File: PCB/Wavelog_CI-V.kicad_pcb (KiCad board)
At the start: 2 copper layers, 28.8 x 55.9 mm, 6 parts, among them SW1 1xUm, X1 CI-V_to_TRX

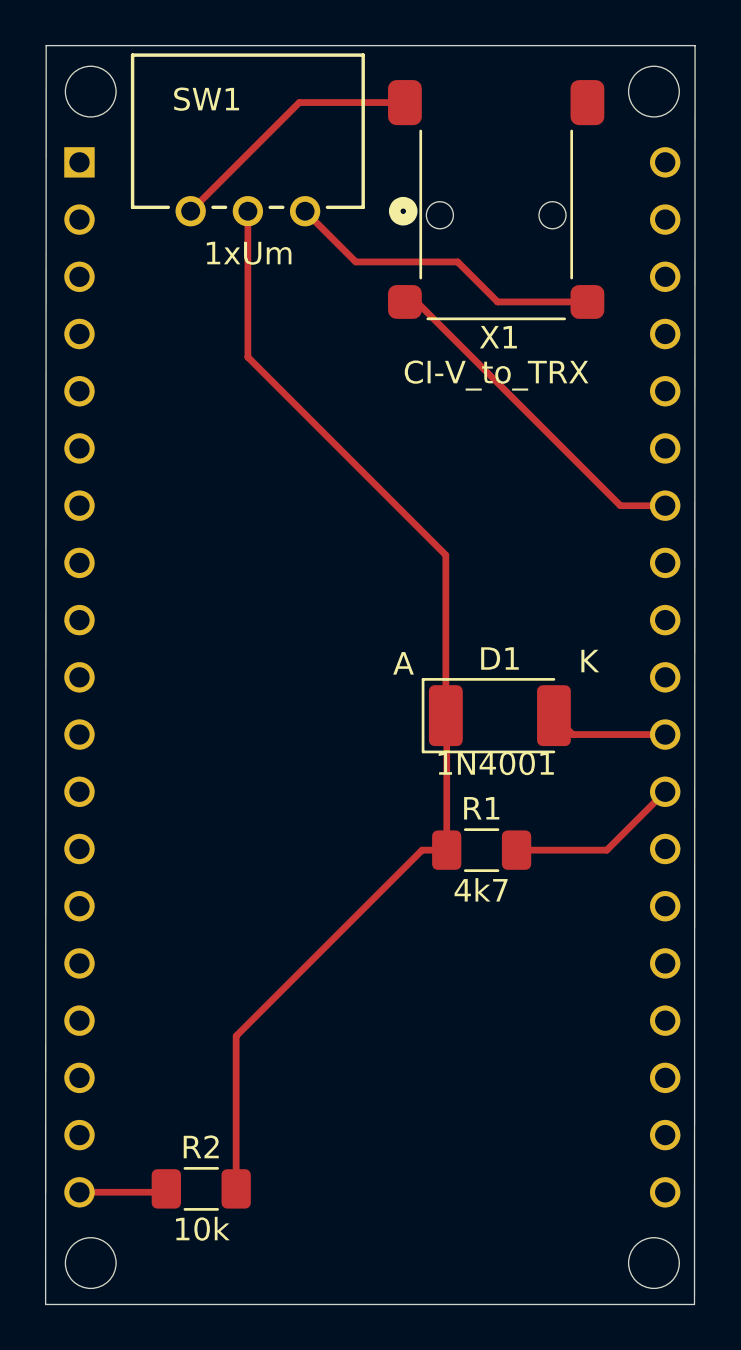
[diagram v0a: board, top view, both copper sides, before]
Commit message: major upgrade PCB v1.2
new features:
++ add 0.96" OLED and RX/TX-LED on PCB and Sketch
++ add rotate button on WebIF for OLED
++ add Autodetect CI-V on Boot
++ add Autodetect button on WebIF
++ add Debug-Level
++ add Debug-Page (last 500 lines or Websocket)
Bugs:
-- Autodetect found no matching address
-- no json-post to WaveLog
-- debug websocket no connection
-- Buffer overflow/Reboot sometimes
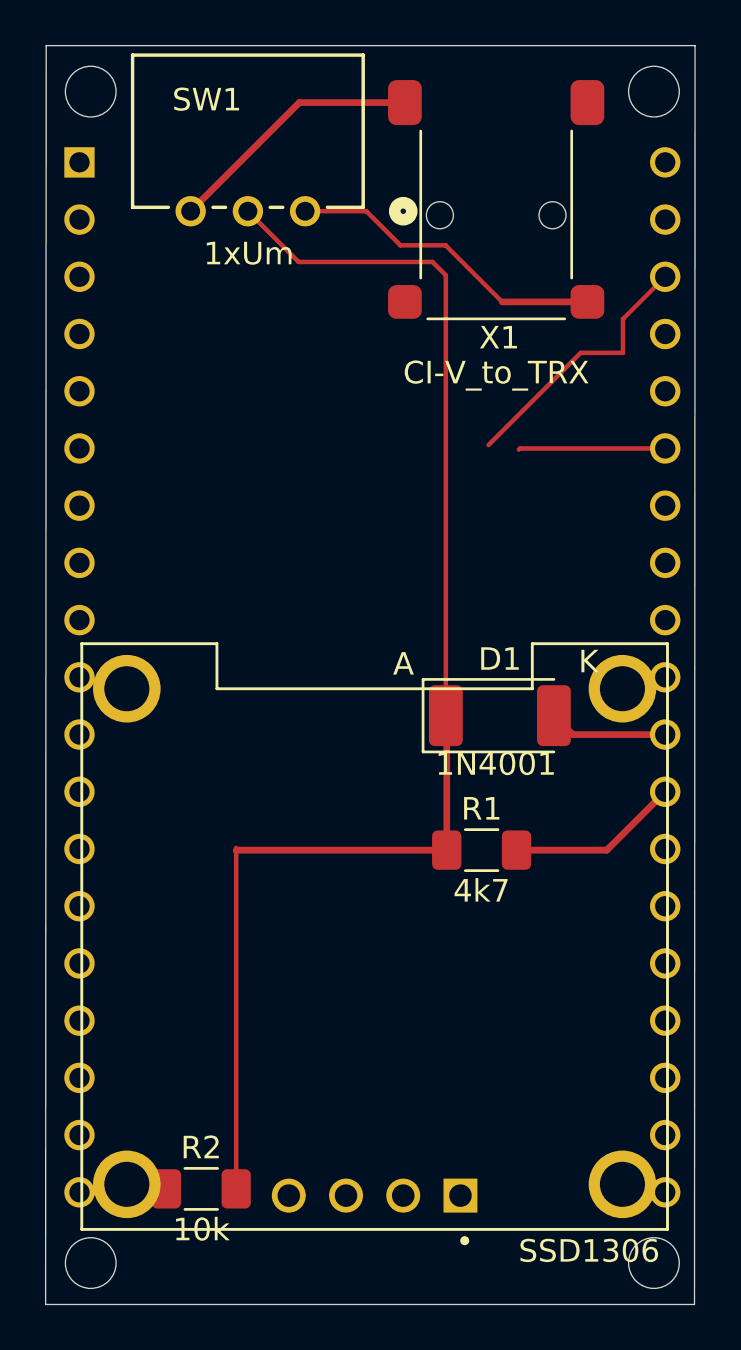
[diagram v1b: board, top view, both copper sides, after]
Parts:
- added SSD1306: MODULE_DM-OLED096-636, footprints:MODULE_DM-OLED096-636, F.Cu at (150.4, 110.9)
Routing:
- net (no net): track 109.6 -> 122.2 mm
